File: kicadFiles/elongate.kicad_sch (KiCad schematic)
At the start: 325 parts, among them J1 TYPE-C-31-M12_13, J2 Conn_ARM_JTAG_SWD_10, J3 Conn_01x6, Q1 AO3401A, Q2 DTC123JKAT146, Q3 AO3400A, Q4 DTC123JKAT146, SW1 MXSwitch, SW10 MXSwitch, SW11 MXSwitch, SW12 MXSwitch, SW13 MXSwitch, SW14 MXSwitch, SW15 MXSwitch, SW16 MXSwitch, SW17 MXSwitch, SW18 MXSwitch, SW19 MXSwitch, SW2 MXSwitch, SW20 MXSwitch, SW21 MXSwitch, SW22 MXSwitch, SW23 MXSwitch, SW24 MXSwitch, SW25 MXSwitch, SW26 MXSwitch, SW27 MXSwitch, SW28 MXSwitch, SW29 MXSwitch, SW3 MXSwitch, SW30 MXSwitch, SW31 MXSwitch, SW32 MXSwitch, SW33 MXSwitch, SW34 MXSwitch, SW35 MXSwitch, SW36 MXSwitch, SW37 MXSwitch, SW38 MXSwitch, SW39 MXSwitch, SW4 MXSwitch, SW40 MXSwitch, SW41 MXSwitch, SW42 MXSwitch, SW43 MXSwitch, SW44 MXSwitch, SW45 MXSwitch, SW46 MXSwitch, SW47 MXSwitch, SW48 MXSwitch, SW49 MXSwitch, SW5 MXSwitch, SW50 MXSwitch, SW51 MXSwitch, SW52 MXSwitch, SW53 MXSwitch, SW54 MXSwitch, SW55 K2-1187SQ-A4SW-06, SW6 MXSwitch, SW7 MXSwitch, SW8 MXSwitch, SW9 MXSwitch, U1 TPD4E05U06DQAR, U2 STM32F072CBT6, U3 MCP1700-3302E

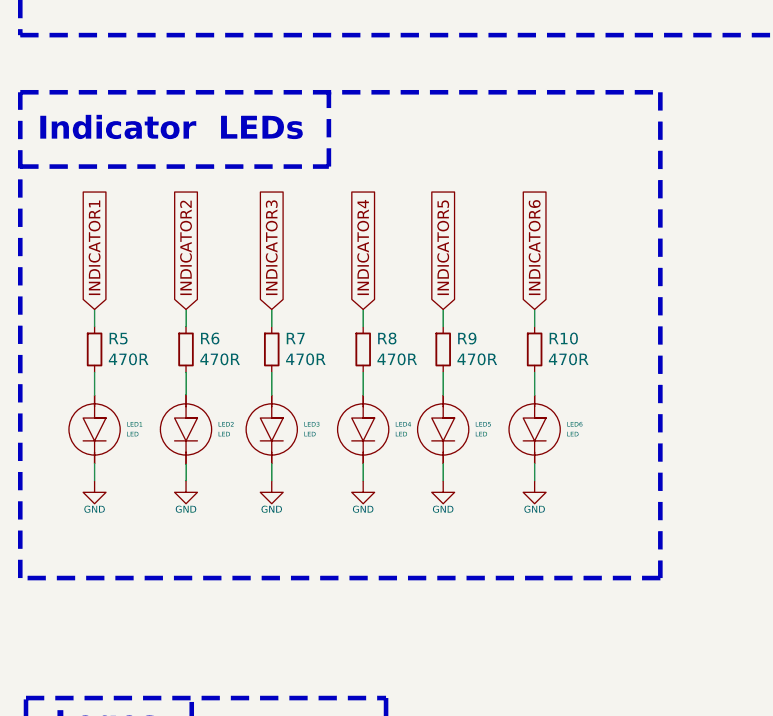
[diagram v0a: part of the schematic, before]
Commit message: Changed indicators as open-collector current sinks
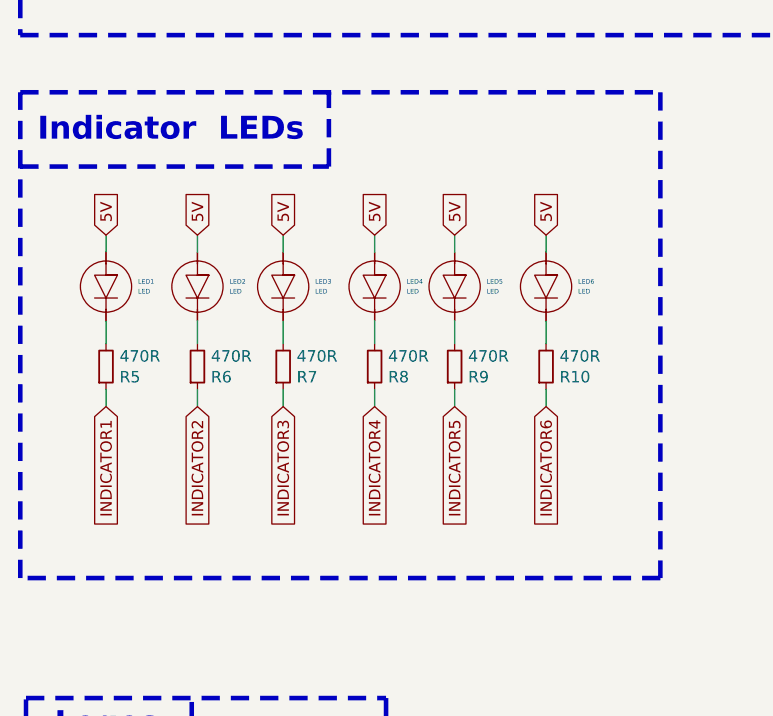
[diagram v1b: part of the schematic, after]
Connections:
- net 5V: now also LED1.A, LED2.A, LED3.A, LED4.A, LED5.A, LED6.A
- net GND: no longer LED1.K, LED2.K, LED3.K, LED4.K, LED5.K, LED6.K
- net at R5.2: now also LED1.K; no longer LED1.A
- net at R6.2: now also LED2.K; no longer LED2.A
- net at R7.2: now also LED3.K; no longer LED3.A
- net at R8.2: now also LED4.K; no longer LED4.A
- net at R9.2: now also LED5.K; no longer LED5.A
- net at R10.2: now also LED6.K; no longer LED6.A
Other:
- moved on the sheet: LED1, LED2, LED3, LED4, LED5, LED6, R10, R5, R6, R7, R8, R9

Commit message: Added new Wurth USBC connector
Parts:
- removed J1: TYPE-C-31-M12_13, acheron_Connectors:TYPE-C-31-M-12, symbol acheronSymbols:TYPE-C-31-M12_13
- added J1: USB_C_Receptacle, symbol acheronSymbols:USB_C_Receptacle
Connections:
- net D+: now also U1.4 (D2+), U1.7 (NC), J1.A6 (D+), J1.B6 (D+); no longer U1.5 (D2-), U1.6 (NC)
- net D-: now also U1.5 (D2-), U1.6 (NC), J1.A7 (D-), J1.B7 (D-); no longer U1.4 (D2+), U1.7 (NC)
- net GND: now also J1.A1 (GND), J1.A12 (GND), J1.B1 (GND), J1.B12 (GND)
- net SHIELD: now also J1.S1 (SHIELD)
- net VBUS: now also J1.A4 (VBUS), J1.A9 (VBUS), J1.B4 (VBUS), J1.B9 (VBUS)
- net at R1.2: now also J1.A5 (CC1)
- net at R2.2: now also J1.B5 (CC2)
- no-connect marks 5 -> 13
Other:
- moved on the sheet: C1, C2, R1, R2, R3, R4

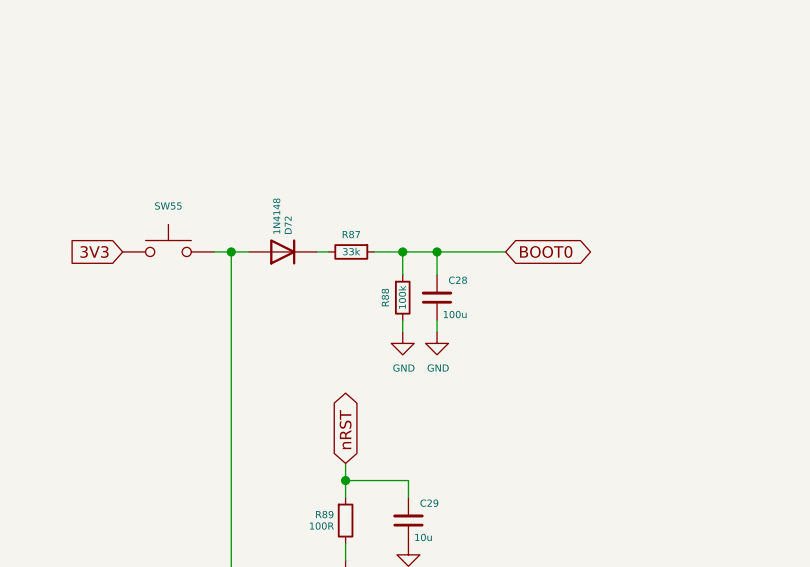
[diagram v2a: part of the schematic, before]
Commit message: Change all silkscreen markings to 25/25/5 mil sizes
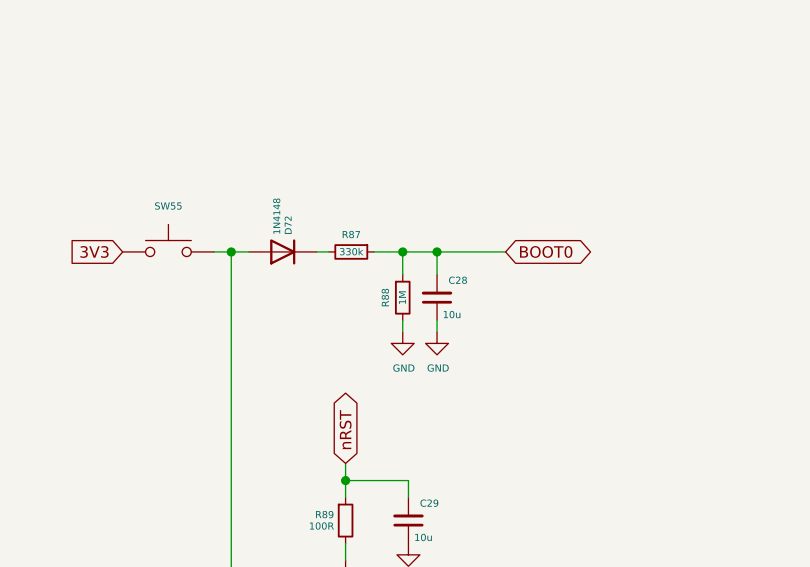
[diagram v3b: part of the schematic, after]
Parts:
- C28: value 100u -> 10u
- R87: value 33k -> 330k
- R88: value 100k -> 1M

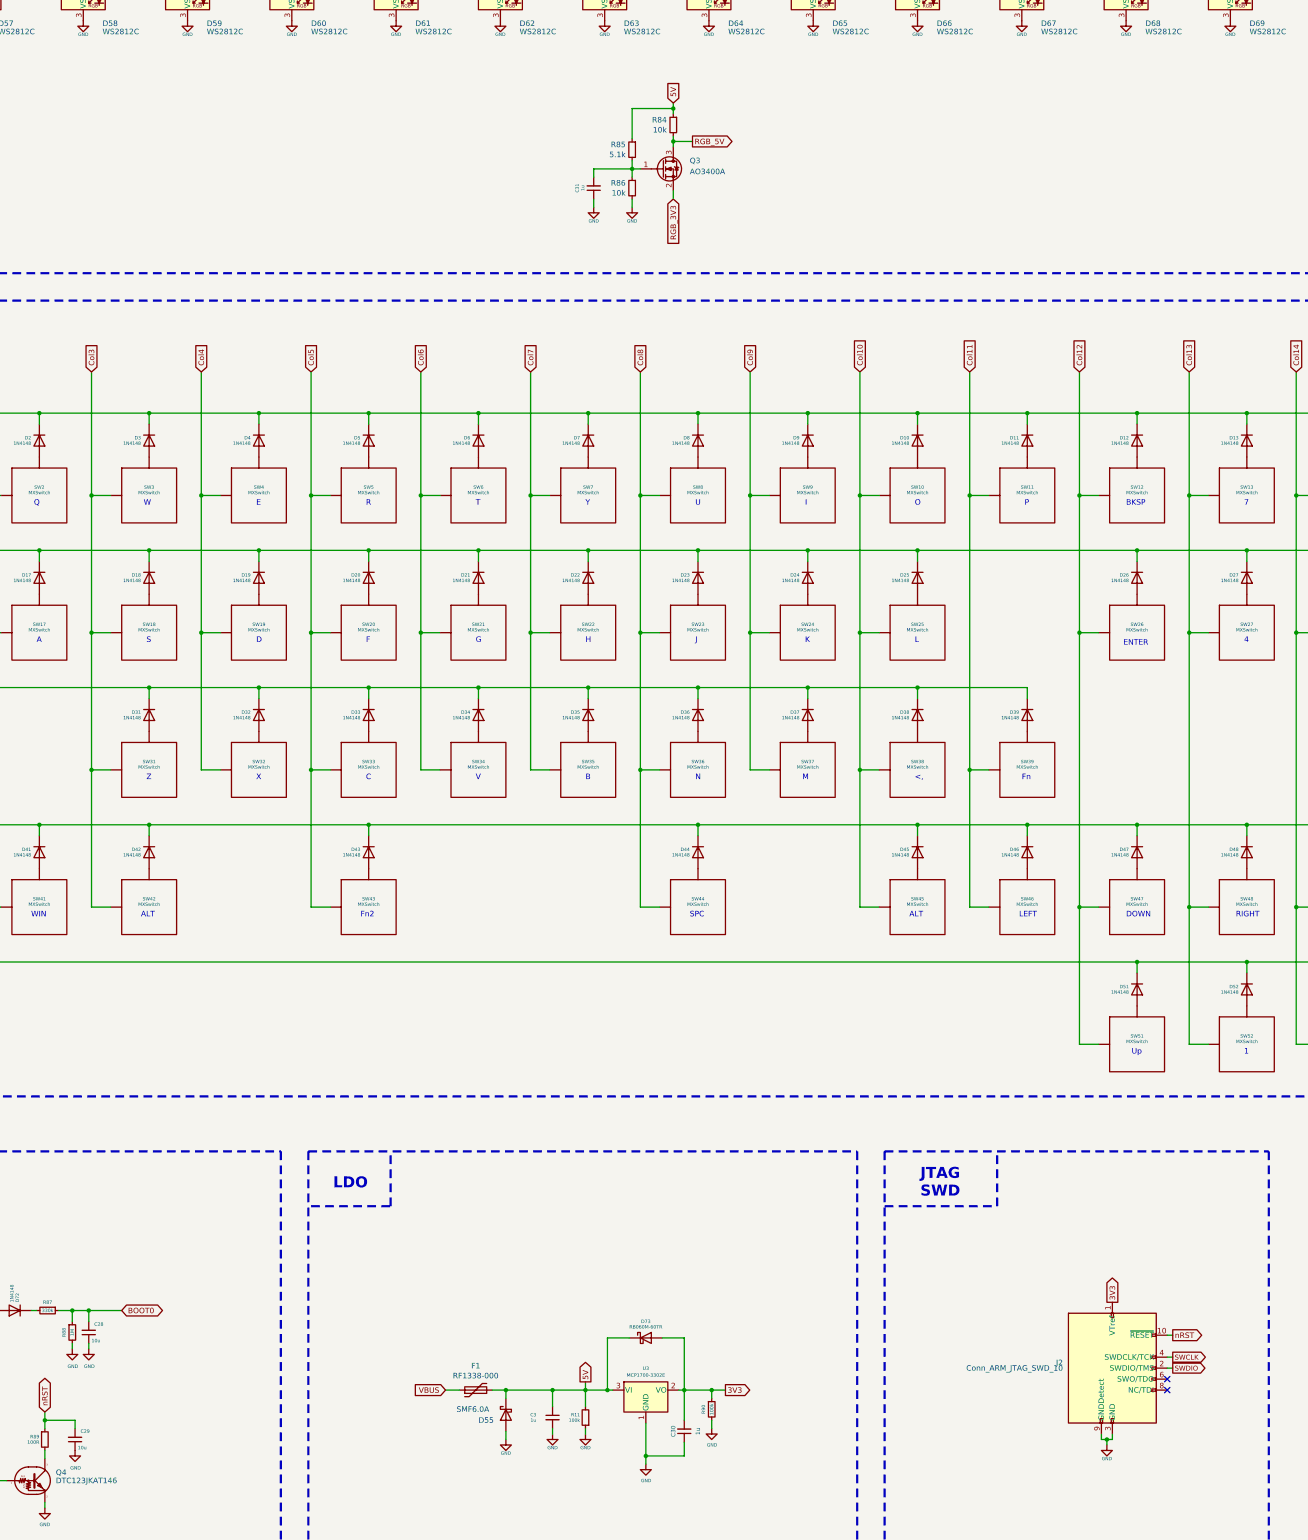
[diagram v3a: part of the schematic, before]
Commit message: Changed SWD for 6-pin equivalent
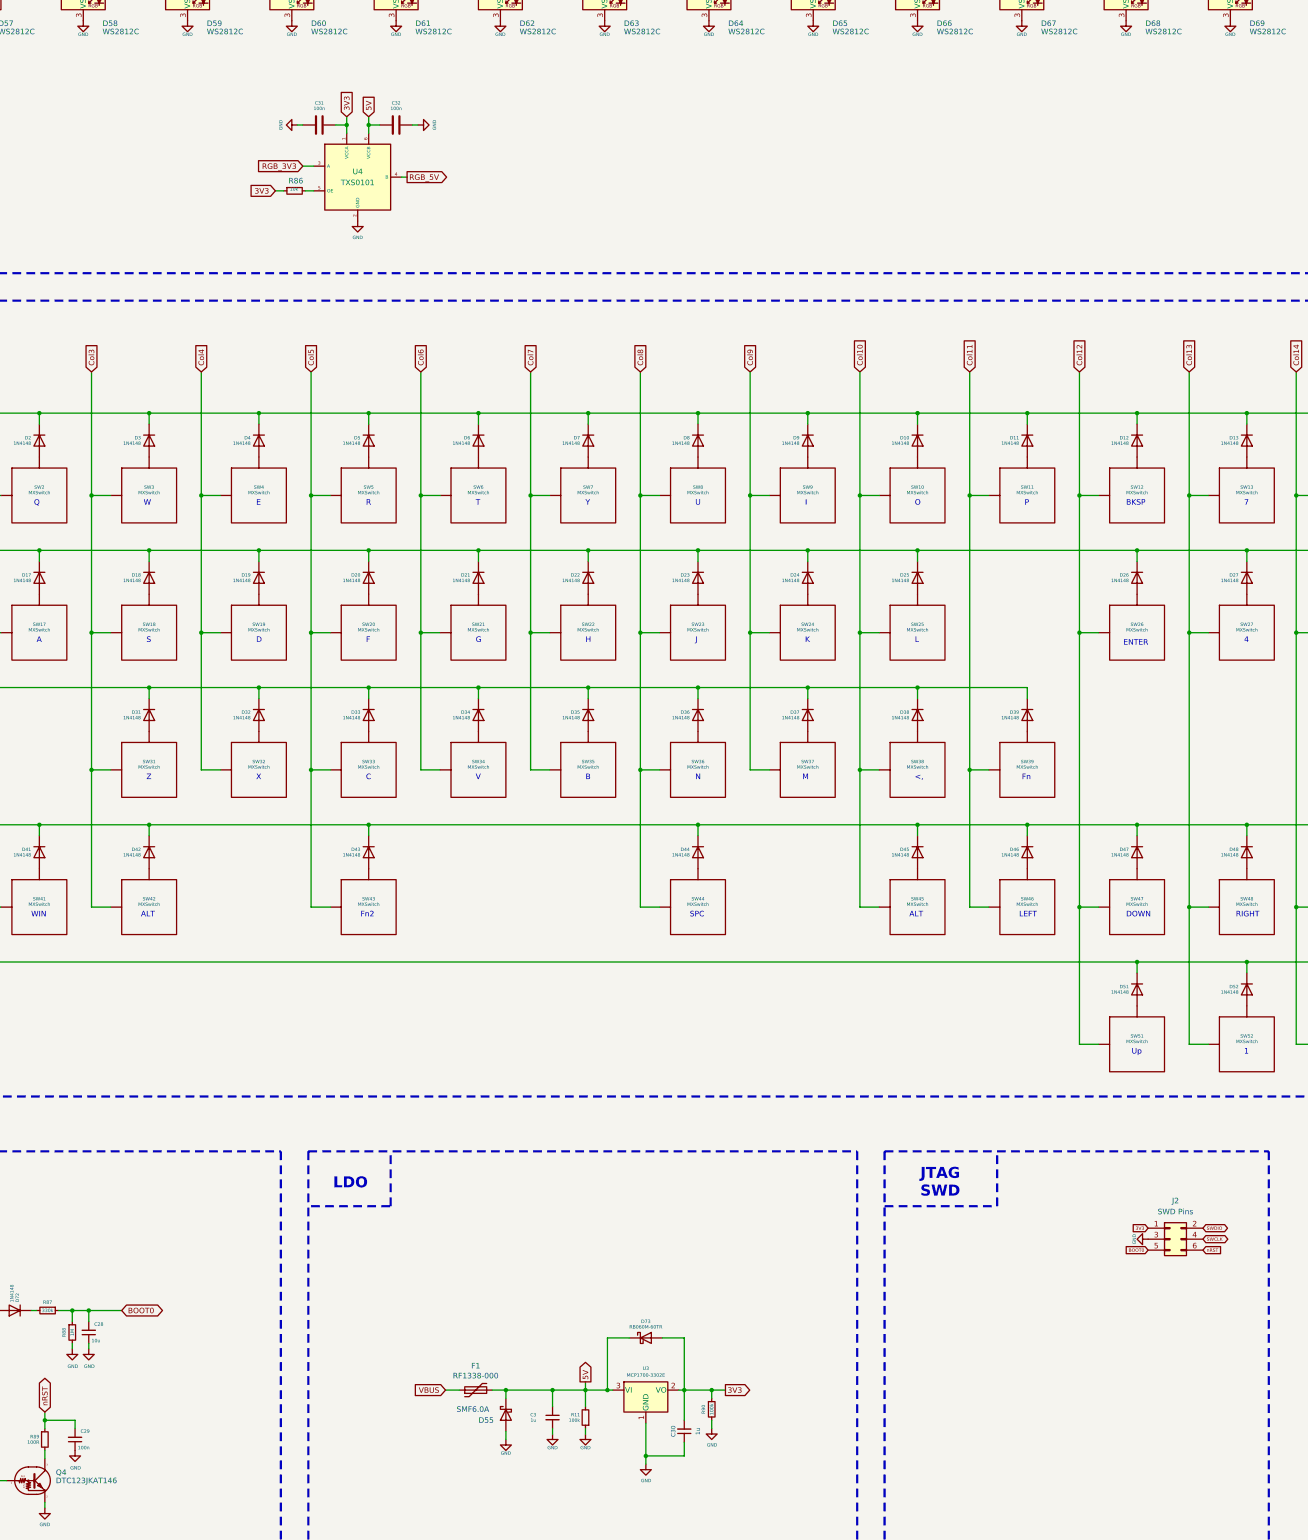
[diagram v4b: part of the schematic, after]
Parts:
- removed C31: 1u, Capacitor_SMD:C_0805_2012Metric, symbol Device:C_Small
- removed J2: Conn_ARM_JTAG_SWD_10, acheron_Connectors:Conn_ARM_JTAG_SWD_10, symbol Connector:Conn_ARM_JTAG_SWD_10
- removed Q3: AO3400A, Package_TO_SOT_SMD:SOT-23, symbol Transistor_FET:AO3400A
- removed R84: 10k, acheron_Components:R_SMD_1206, symbol Device:R_Small
- removed R85: 5.1k, acheron_Components:R_SMD_1206, symbol Device:R_Small
- added C31, C32: 100n, Capacitor_SMD:C_0805_2012Metric, symbol Device:C
- added J2: SWD Pins, acheron_Connectors:PinHeader_2x3_P2.54mm_Vertical, symbol Connector_Generic:Conn_02x03_Odd_Even
- added U4: TXS0101, acheron_Components:SOT-23-6, symbol acheronSymbols:TXS0101
- C29: value 10u -> 100n
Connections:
- net 3V3: now also R86.1, C31.2, J2.1 (Pin_1), U4.1 (VCCA)
- net 5V: now also C32.1, U4.6 (VCCB)
- net BOOT0: now also J2.5 (Pin_5)
- net GND: now also C31.1, C32.2, J2.3 (Pin_3), U4.2 (GND); no longer R86.2
- net RGB_3V3: now also U4.3 (A)
- net RGB_5V: now also U4.4 (B)
- net SWCLK: now also J2.4 (Pin_4)
- net SWDIO: now also J2.2 (Pin_2)
- net nRST: now also J2.6 (Pin_6)
- new net: R86.2, U4.5 (OE)
- no-connect marks 13 -> 11
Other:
- moved on the sheet: R86

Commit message: Change LDO regulating caps to tantallums
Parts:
- removed C30: 1u, Capacitor_SMD:C_0805_2012Metric_Pad1.15x1.40mm_HandSolder, symbol Device:C_Small
- added C30: 1u, acheron_Components:CP_EIA-3216-10_Kemet-I_Pad1.58x1.35mm_HandSolder, symbol Device:CP1_Small
- C3: footprint Capacitor_SMD:C_0805_2012Metric_Pad1.15x1.40mm_HandSolder -> acheron_Components:CP_EIA-3216-10_Kemet-I_Pad1.58x1.35mm_HandSolder; symbol Device:C_Small -> Device:CP1_Small; Package C0805 -> C3216
- J1: footprint (none) -> acheron_Connectors:USB_C_Receptacle_Wurth_Elektronik_632723x00011
- R10, R14, R15, R16, R17, R18, R19, R20, R21, R22, R23, R24, R25, R26, R27, R28, R29, R30, R31, R32, R33, R34, R35, R36, R37, R38, R39, R40, R41, R42, R43, R44, R45, R46, R47, R48, R49, R5, R50, R51, R52, R53, R54, R55, R56, R57, R58, R59, R6, R60, R61, R62, R63, R64, R65, R66, R67, R7, R8, R9: value 470R -> 470
- R68, R69, R70, R71, R72, R73, R74, R75, R76, R77, R78, R79, R80, R81, R82, R83: value 3R -> 4.7
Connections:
- net 3V3: now also C30.1
- net GND: now also C30.2

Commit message: Add metadata to connector, move RCC resistors
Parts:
- C28, C29: Package (none) -> C0805
- J1: value USB_C_Receptacle -> Wurth 632723300011; Manufacturer (none) -> Wurth Elektronik; Manufacturer Part Number (none) -> 632723300011
- R1, R2: footprint Resistor_SMD:R_0402_1005Metric -> acheron_Components:R_SMD_1206
- R87, R88, R89: Package (none) -> R1206
- SW1, SW10, SW11, SW12, SW13, SW14, SW15, SW17, SW18, SW19, SW2, SW20, SW21, SW22, SW23, SW24, SW25, SW27, SW28, SW29, SW3, SW31, SW32, SW33, SW34, SW35, SW36, SW37, SW38, SW4, SW41, SW45, SW46, SW47, SW48, SW49, SW5, SW50, SW51, SW52, SW53, SW54, SW6, SW7, SW8, SW9: value MXSwitch -> MX100
- SW16, SW39, SW40, SW42: value MXSwitch -> MX125
- SW26, SW30: value MXSwitch -> MX175
- SW43: value MXSwitch -> MX225
- SW44: value MXSwitch -> MX275
- renumbered L1 to GR1, L2 to GR2, L3 to GR3, L4 to GR4, L5 to GR5

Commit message: DRC ran, new label
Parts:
- R89: value 100R -> 100
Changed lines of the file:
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@@
     (title "ElongatePCB")
     (date "2021-01-29")
-    (rev "V3.2.4")
+    (rev "pre-Delta")
     (company "Designed by Gondolindrim")
     (comment 1 "In partnership with MrKeebs and 159")
@@
       (effects (font (size 0.7874 0.7874)) (justify right))
     )
-    (property "Value" "100R" (id 1) (at 223.52 384.81 0)
+    (property "Value" "100" (id 1) (at 223.52 384.81 0)
       (effects (font (size 0.7874 0.7874)) (justify right))
     )
@@
     )
     (path "/633929d2-01b6-473b-8d21-cc19b081102d"
-      (reference "R89") (unit 1) (value "100R") (footprint "acheron_Components:R_SMD_1206")
+      (reference "R89") (unit 1) (value "100") (footprint "acheron_Components:R_SMD_1206")
     )
     (path "/00000000-0000-0000-0000-00005e0e3a96"

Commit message: Updated fills, DRC ran, erros corrected
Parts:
- D72: renamed from D73; Manufacturer Part Number RB060M-60TR -> (none)
- LED1: renamed from LED7; now left out of the parts list
- LED10: renamed from LED16; now left out of the parts list
- LED11: renamed from LED17; now left out of the parts list
- LED12: renamed from LED18; now left out of the parts list
- LED13: renamed from LED19; now left out of the parts list
- LED14: renamed from LED20; now left out of the parts list
- LED15: renamed from LED21; now left out of the parts list
- LED16: renamed from LED22; now left out of the parts list
- LED17: renamed from LED23; now left out of the parts list
- LED18: renamed from LED24; now left out of the parts list
- LED19: renamed from LED25; now left out of the parts list
- LED2: renamed from LED8; now left out of the parts list
- LED20: renamed from LED26; now left out of the parts list
- LED21: renamed from LED27; now left out of the parts list
- LED22: renamed from LED28; now left out of the parts list
- LED23: renamed from LED29; now left out of the parts list
- LED24: renamed from LED30; now left out of the parts list
- LED25: renamed from LED31; now left out of the parts list
- LED26: renamed from LED32; now left out of the parts list
- LED27: renamed from LED33; now left out of the parts list
- LED28: renamed from LED34; now left out of the parts list
- LED29: renamed from LED35; now left out of the parts list
- LED3: renamed from LED9; now left out of the parts list
- LED30: renamed from LED36; now left out of the parts list
- LED31: renamed from LED37; now left out of the parts list
- LED32: renamed from LED38; now left out of the parts list
- LED33: renamed from LED39; now left out of the parts list
- LED34: renamed from LED40; now left out of the parts list
- LED35: renamed from LED41; now left out of the parts list
- LED36: renamed from LED42; now left out of the parts list
- LED37: renamed from LED43; now left out of the parts list
- LED38: renamed from LED44; now left out of the parts list
- LED39: renamed from LED45; now left out of the parts list
- LED4: renamed from LED10; now left out of the parts list
- LED40: renamed from LED46; now left out of the parts list
- LED41: renamed from LED47; now left out of the parts list
- LED42: renamed from LED48; now left out of the parts list
- LED43: renamed from LED49; now left out of the parts list
- LED44: renamed from LED50; now left out of the parts list
- LED45: renamed from LED51; now left out of the parts list
- LED46: renamed from LED52; now left out of the parts list
- LED47: renamed from LED53; now left out of the parts list
- LED48: renamed from LED54; now left out of the parts list
- LED49: renamed from LED55; now left out of the parts list
- LED5: renamed from LED11; now left out of the parts list
- LED50: renamed from LED56; now left out of the parts list
- LED51: renamed from LED57; now left out of the parts list
- LED52: renamed from LED58; now left out of the parts list
- LED53: renamed from LED59; now left out of the parts list
- LED54: renamed from LED60; now left out of the parts list
- LED55: renamed from LED1; now left out of the parts list
- LED56: renamed from LED2; now left out of the parts list
- LED57: renamed from LED3; now left out of the parts list
- LED58: renamed from LED4; now left out of the parts list
- LED59: renamed from LED5; now left out of the parts list
- LED6: renamed from LED12; now left out of the parts list
- LED60: renamed from LED6; now left out of the parts list
- LED7: renamed from LED13; now left out of the parts list
- LED8: renamed from LED14; now left out of the parts list
- LED9: renamed from LED15; now left out of the parts list
- U4: renamed from U3; value MCP1700-3302E -> MCP1700T-3302E/TT; Manufacturer Part Number MCP1700-3302E/TT -> (none)
- X2: renamed from J2; now left out of the parts list
- renumbered C12 to C1, C21 to C10, C22 to C11, C23 to C12, C24 to C13, C25 to C14, C26 to C15, C27 to C16, C4 to C17, C5 to C18, C6 to C19, C13 to C2, C7 to C20, C31 to C21, C32 to C22, C8 to C23, C9 to C24, C10 to C25, C11 to C26, C1 to C27, C2 to C28, C28 to C29, C14 to C3, C3 to C30, C30 to C31, C29 to C32, C15 to C4, C16 to C5, C17 to C6, C18 to C7, C19 to C8, C20 to C9, D56 to D1, D65 to D10, D66 to D11, D67 to D12, D68 to D13, D69 to D14, D70 to D15, D71 to D16, D1 to D17, D2 to D18, D3 to D19, D57 to D2, D4 to D20, D5 to D21, D6 to D22, D7 to D23, D8 to D24, D9 to D25, D10 to D26, D11 to D27, D12 to D28, D13 to D29, D58 to D3, D14 to D30, D15 to D31, D16 to D32, D17 to D33, D18 to D34, D19 to D35, D20 to D36, D21 to D37, D22 to D38, D23 to D39, D59 to D4, D24 to D40, D25 to D41, D26 to D42, D27 to D43, D28 to D44, D29 to D45, D30 to D46, D31 to D47, D32 to D48, D33 to D49, D60 to D5, D34 to D50, D35 to D51, D36 to D52, D37 to D53, D38 to D54, D39 to D55, D40 to D56, D41 to D57, D42 to D58, D43 to D59, D61 to D6, D44 to D60, D45 to D61, D46 to D62, D47 to D63, D48 to D64, D49 to D65, D50 to D66, D51 to D67, D52 to D68, D53 to D69, D62 to D7, D54 to D70, D72 to D71, D55 to D73, D63 to D8, D64 to D9, Q4 to Q3, R68 to R1, R77 to R10, R78 to R11, R79 to R12, R80 to R13, R81 to R14, R82 to R15, R83 to R16, R12 to R17, R13 to R18, R14 to R19, R69 to R2, R15 to R20, R16 to R21, R17 to R22, R18 to R23, R19 to R24, R20 to R25, R21 to R26, R22 to R27, R23 to R28, R24 to R29, R70 to R3, R25 to R30, R26 to R31, R27 to R32, R28 to R33, R86 to R34, R29 to R35, R30 to R36, R31 to R37, R32 to R38, R33 to R39, R71 to R4, R34 to R40, R35 to R41, R36 to R42, R37 to R43, R38 to R44, R39 to R45, R40 to R46, R41 to R47, R42 to R48, R43 to R49, R72 to R5, R44 to R50, R45 to R51, R46 to R52, R47 to R53, R48 to R54, R49 to R55, R50 to R56, R51 to R57, R52 to R58, R53 to R59, R73 to R6, R54 to R60, R55 to R61, R56 to R62, R57 to R63, R58 to R64, R59 to R65, R60 to R66, R61 to R67, R62 to R68, R63 to R69, R74 to R7, R64 to R70, R65 to R71, R66 to R72, R67 to R73, R1 to R74, R2 to R75, R3 to R76, R4 to R77, R5 to R78, R6 to R79, R75 to R8, R7 to R80, R8 to R81, R9 to R82, R10 to R83, R87 to R84, R88 to R85, R90 to R86, R11 to R87, R89 to R88, R76 to R9, U4 to U1, U1 to U3, J3 to X1
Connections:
- net 5V: no longer D73.1 (K), LED55.A, LED56.A, LED57.A, LED58.A, LED59.A, LED60.A
- net VBUS: now also D73.1 (K)
- net LED_BRIGHTNESS: now reaches Q1.3 (D), R19.1, R20.1, R21.1, R22.1, R23.1, R24.1, R25.1, R26.1, R27.1, R28.1, R29.1, R30.1, R31.1, R32.1, R33.1, R35.1, R36.1, R37.1, R38.1, R39.1, R40.1, R41.1, R42.1, R43.1, R44.1, R45.1, R46.1, R47.1, R48.1, R49.1, R50.1, R51.1, R52.1, R53.1, R54.1, R55.1, R56.1, R57.1, R58.1, R59.1, R60.1, R61.1, R62.1, R63.1, R64.1, R65.1, R66.1, R67.1, R68.1, R69.1, R70.1, R71.1, R72.1, R73.1
- net LED_BRIGHTNESS: now also LED55.A, LED56.A, LED57.A, LED58.A, LED59.A, LED60.A
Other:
- moved on the sheet: D73, F1
